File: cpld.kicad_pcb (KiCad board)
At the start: 2 copper layers, 30 parts, among them IC1 MCP1726-3302E_SN, IC2 EPM3064ATC44-7N, J1 USB_OTG, J2 INPUTS, J3 OUTPUTS, J4 Conn_ARM_JTAG_SWD_10, SW1 POWER_SW, SW2 SW_DIP_x01, SW3 SW_DIP_x01, SW4 SW_DIP_x01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

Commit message: Final PCB
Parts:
- removed SW4, SW5: SW_DIP_x01, Button_Switch_THT:SW_DIP_SPSTx01_Slide_9.78x4.72mm_W7.62mm_P2.54mm
- added C9: 0.1u, Capacitor_SMD:C_0603_1608Metric, F.Cu at (152.2, 93.3)
- added SW0: SW_DIP_x01, Button_Switch_THT:SW_DIP_SPSTx01_Slide_9.78x4.72mm_W7.62mm_P2.54mm, F.Cu at (180.3, 119.3)
- added SW_POW1: POWER_SW, Button_Switch_THT:SW_DIP_SPSTx01_Slide_9.78x4.72mm_W7.62mm_P2.54mm, F.Cu at (103.3, 107.7)
- C2: value 1000p -> 1u
- J2, J3: footprint Connector_PinSocket_2.54mm:PinSocket_2x16_P2.54mm_Vertical -> Connector_PinSocket_2.54mm:PinSocket_2x16_P2.54mm_Vertical_SMD; moved to B.Cu
- SW1: value POWER_SW -> SW_DIP_x01
- Y1: value ECS-2033-500-BN-TR3 -> ECS-TXO-3225-250-TR; footprint ECS2033:ECS2033500BNTR3 -> ECS_3225:OSC_ECS-TXO-3225-250-TR
- moved R6 61.1 mm to (123.3, 118.9), turned to -90 degrees
- moved SW1 55.1 mm to (170.3, 119.3), turned to 90 degrees
- moved J3 54.4 mm to (169.8, 68.0), turned to -90 degrees
- moved R7 50.9 mm to (170.3, 102.7), turned to -90 degrees
- moved SW2 49.0 mm to (160.3, 119.3), turned to 90 degrees
- moved D2 48.8 mm to (165.2, 101.8), turned to -90 degrees
- moved SW3 45.3 mm to (150.3, 119.3), turned to 90 degrees
- moved J1 44.5 mm to (91.0, 102.9), turned to -90 degrees
- moved R1 39.0 mm to (113.2, 102.4), turned to 90 degrees
- moved C2 27.0 mm to (129.2, 102.1), turned to 90 degrees
- moved R4 26.8 mm to (124.2, 87.0), turned to 90 degrees
- moved R3 25.8 mm to (121.2, 87.0), turned to -90 degrees
- moved R8 24.8 mm to (138.9, 98.0), turned to -90 degrees
- moved C4 23.8 mm to (138.9, 101.6), turned to -90 degrees
- moved C1 23.4 mm to (96.2, 100.8), turned to -90 degrees
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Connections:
- D1 pad 1: GND -> Net-(D1-Pad1)
- D1 pad 2: Net-(D1-Pad2) -> /POWER_LED
- D2 pad 1: GND -> Net-(D2-Pad1)
- D2 pad 2: Net-(D2-Pad2) -> /STATUS_LED
- IC2 pad 1: /TDI -> /DI0/TDI
- IC2 pad 10: /DI5 -> /DI7
- IC2 pad 12: /DI6 -> /DI8
- IC2 pad 13: /DI7 -> /DI9
- IC2 pad 14: /DI8 -> /DI10
- IC2 pad 15: /DI9 -> /DI11
- IC2 pad 18: /DO0 -> /DI12
- IC2 pad 19: /DO1 -> /DO0
- IC2 pad 2: /DI0 -> /DI1
- IC2 pad 20: /DO2 -> /DO1
- IC2 pad 21: /DO3 -> /DO2
- IC2 pad 22: /DO4 -> /DO3
- IC2 pad 23: /DO5 -> /DO4
- IC2 pad 25: /DO6 -> /DO5
- IC2 pad 26: /TCK -> /DO6/TCK
- IC2 pad 28: /DO8 -> /DO9
- IC2 pad 3: /DI1 -> /DI2
- IC2 pad 31: /DO9 -> /DO10
- IC2 pad 32: /TDO -> /DO11/TDO
- IC2 pad 33: unconnected-(IC2-Pad33) -> /DO12
- IC2 pad 34: /SW_B0 -> /STATUS_LED
- IC2 pad 35: /SW_B1 -> /SW_B0
- IC2 pad 42: /SW_B2 -> /SW_B1
- IC2 pad 43: /SW_B3 -> /SW_B2
- IC2 pad 44: unconnected-(IC2-Pad44) -> /SW_B3
- IC2 pad 5: /DI2 -> /DI3
- IC2 pad 6: /DI3 -> /DI4
- IC2 pad 7: /TMS -> /DI5/TMS
- IC2 pad 8: /DI4 -> /DI6
- J2 pad 1: /DI0 -> /DI0/TDI
- J2 pad 10: /DI9 -> GND
- J2 pad 11: unconnected-(J2-Pad11) -> /DI5/TMS
- J2 pad 12: unconnected-(J2-Pad12) -> GND
- J2 pad 13: unconnected-(J2-Pad13) -> /DI6
- J2 pad 14: unconnected-(J2-Pad14) -> GND
- J2 pad 15: unconnected-(J2-Pad15) -> /DI7
- J2 pad 16: unconnected-(J2-Pad16) -> GND
- J2 pad 17: GND -> /DI8
- J2 pad 19: GND -> /DI9
- J2 pad 2: /DI1 -> GND
- J2 pad 21: GND -> /DI10
- J2 pad 23: GND -> /DI11
- J2 pad 25: GND -> /DI12
- J2 pad 27: GND -> unconnected-(J2-Pad27)
- J2 pad 29: GND -> unconnected-(J2-Pad29)
- J2 pad 3: /DI2 -> /DI1
- J2 pad 31: GND -> unconnected-(J2-Pad31)
- J2 pad 4: /DI3 -> GND
- J2 pad 5: /DI4 -> /DI2
- J2 pad 6: /DI5 -> GND
- J2 pad 7: /DI6 -> /DI3
- J2 pad 8: /DI7 -> GND
- J2 pad 9: /DI8 -> /DI4
- J3 pad 10: /DO9 -> GND
- J3 pad 11: unconnected-(J3-Pad11) -> /DO5
- J3 pad 12: unconnected-(J3-Pad12) -> GND
- J3 pad 13: unconnected-(J3-Pad13) -> /DO6/TCK
- J3 pad 14: unconnected-(J3-Pad14) -> GND
- J3 pad 15: unconnected-(J3-Pad15) -> /DO7
- J3 pad 16: unconnected-(J3-Pad16) -> GND
- J3 pad 17: GND -> /DO8
- J3 pad 19: GND -> /DO9
- J3 pad 2: /DO1 -> GND
- J3 pad 21: GND -> /DO10
- J3 pad 23: GND -> /DO11/TDO
- J3 pad 25: GND -> /DO12
- J3 pad 27: GND -> unconnected-(J3-Pad27)
- J3 pad 29: GND -> unconnected-(J3-Pad29)
- J3 pad 3: /DO2 -> /DO1
- J3 pad 31: GND -> unconnected-(J3-Pad31)
- J3 pad 4: /DO3 -> GND
- J3 pad 5: /DO4 -> /DO2
- J3 pad 6: /DO5 -> GND
- J3 pad 7: /DO6 -> /DO3
- J3 pad 8: /DO7 -> GND
- J3 pad 9: /DO8 -> /DO4
- J4 pad 2: /TMS -> /DI5/TMS
- J4 pad 4: /TCK -> /DO6/TCK
- J4 pad 8: /TDI -> /DI0/TDI
- R2 pad 2: /TDO -> /DO11/TDO
- R3 pad 1: /TMS -> /DI5/TMS
- R4 pad 2: /TDO -> /DO11/TDO
- R5 pad 2: /TDI -> /DI0/TDI
- R6 pad 1: /POWER_LED -> Net-(D1-Pad1)
- R6 pad 2: Net-(D1-Pad2) -> GND
- R7 pad 1: /STATUS_LED -> Net-(D2-Pad1)
- R7 pad 2: Net-(D2-Pad2) -> GND
- R8 pad 1: /TCK -> /DO6/TCK
- SW1 pad 2: Net-(IC1-Pad3) -> /SW_B1
- SW2 pad 2: /SW_B0 -> /SW_B2
- SW3 pad 2: /SW_B1 -> /SW_B3
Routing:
- net +3.3V: track 0.00 -> 112.3 mm
- net /DI0/TDI: track 0.00 -> 108.6 mm, vias 0 -> 3
- net /DO11/TDO: track 0.00 -> 93.1 mm, vias 0 -> 5
- net /DO6/TCK: track 0.00 -> 90.2 mm, vias 0 -> 5
- net /DI5/TMS: track 0.00 -> 82.0 mm, vias 0 -> 3
- net GND: track 0.00 -> 72.2 mm, vias 0 -> 88
- net /DI1: track 0.00 -> 66.7 mm, vias 0 -> 1
- net /DI2: track 0.00 -> 64.2 mm, vias 0 -> 1
- net /DI3: track 0.00 -> 60.0 mm, vias 0 -> 1
- net /DO12: track 0.00 -> 57.8 mm, vias 0 -> 3
- net /DO5: track 0.00 -> 57.4 mm, vias 0 -> 3
- net /DO4: track 0.00 -> 57.0 mm, vias 0 -> 3
- net /DI4: track 0.00 -> 56.3 mm, vias 0 -> 1
- net /DO7: track 0.00 -> 55.9 mm, vias 0 -> 3
- net /DO10: track 0.00 -> 55.4 mm, vias 0 -> 3
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- added copper zone on B.Cu, net GND
- added copper zone on F.Cu, net GND
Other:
- board outline added: 105 x 72 mm

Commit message: Improved PCB layout
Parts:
- C9, IC2, Y1: moved to B.Cu
- J4: footprint Connector_PinSocket_2.54mm:PinSocket_2x05_P2.54mm_Vertical -> Connector_PinSocket_2.54mm:PinSocket_2x05_P2.54mm_Vertical_SMD
- moved SW0 48.7 mm to (183.8, 83.9), turned to -90 degrees
- moved R7 47.5 mm to (125.1, 87.9), turned to 0 degrees
- moved D2 46.6 mm to (120.8, 87.9), turned to 180 degrees
- moved SW3 44.2 mm to (153.8, 83.9), turned to -90 degrees
- moved SW1 37.9 mm to (173.8, 83.9), turned to -90 degrees
- moved R6 36.5 mm to (104.0, 87.9), turned to 180 degrees
- moved SW2 36.0 mm to (163.8, 83.9), turned to -90 degrees
- moved R4 32.0 mm to (147.3, 64.9), turned to -90 degrees
- moved R2 31.1 mm to (147.3, 68.3), turned to 90 degrees
- moved J4 30.3 mm to (141.1, 69.1), turned to 180 degrees
- moved D1 30.3 mm to (107.9, 87.9), turned to 0 degrees
- moved SW_POW1 25.5 mm to (99.4, 82.5)
- moved R1 23.6 mm to (110.7, 79.0)
- moved J1 23.4 mm to (91.2, 79.5)
- moved C1 23.4 mm to (96.0, 77.4)
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- renumbered SW3 to SW0, SW2 to SW1, SW1 to SW2, SW0 to SW3
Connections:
- D1 pad 2: /POWER_LED -> +5V
- IC1 pad 5: /POWER_LED -> /STATUS_LED
- IC2 pad 28: /DO9 -> /DO8
- IC2 pad 31: /DO10 -> /DO9
- IC2 pad 32: /DO11/TDO -> /DO10/TDO
- IC2 pad 33: /DO12 -> /DO11
- IC2 pad 34: /STATUS_LED -> /DO12
- IC2 pad 35: /SW_B0 -> /SW_B3
- IC2 pad 42: /SW_B1 -> /SW_B2
- IC2 pad 43: /SW_B2 -> /SW_B1
- IC2 pad 44: /SW_B3 -> /SW_B0
- J3 pad 21: /DO10 -> /DO10/TDO
- J3 pad 23: /DO11/TDO -> /DO11
- R2 pad 2: /DO11/TDO -> /DO10/TDO
- R4 pad 2: /DO11/TDO -> /DO10/TDO
- SW0 pad 2: /SW_B3 -> /SW_B0
- SW1 pad 2: /SW_B2 -> /SW_B1
- SW2 pad 2: /SW_B1 -> /SW_B2
- SW3 pad 2: /SW_B0 -> /SW_B3
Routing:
- net /DO11/TDO: track 93.1 -> 0.00 mm, vias 5 -> 0
- net /DO10/TDO: track 0.00 -> 75.9 mm, vias 0 -> 1
- net /DO10: track 55.4 -> 0.00 mm, vias 3 -> 0
- net /DO11: track 0.00 -> 46.1 mm
- net /SW_B3: track 53.3 -> 13.1 mm, vias 1 -> 0
- net /DO8: track 0.00 -> 35.9 mm
- net /DO4: track 57.0 -> 23.4 mm, vias 3 -> 0
- net /DO6/TCK: track 90.2 -> 57.7 mm, vias 5 -> 2
- net /DO5: track 57.4 -> 27.2 mm, vias 3 -> 0
- net /DO0: track 43.3 -> 14.0 mm, vias 3 -> 0
- net /DO1: track 42.6 -> 15.9 mm, vias 3 -> 0
- net /DO2: track 42.2 -> 17.8 mm, vias 3 -> 0
- net /DO7: track 55.9 -> 33.2 mm, vias 3 -> 0
- net /DO3: track 41.8 -> 19.7 mm, vias 3 -> 0
- net +3.3V: track 112.3 -> 91.2 mm, vias 0 -> 4
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- added copper zone on F.Cu, net +3.3V
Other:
- board size 105 x 72 mm -> 105 x 42.1 mm

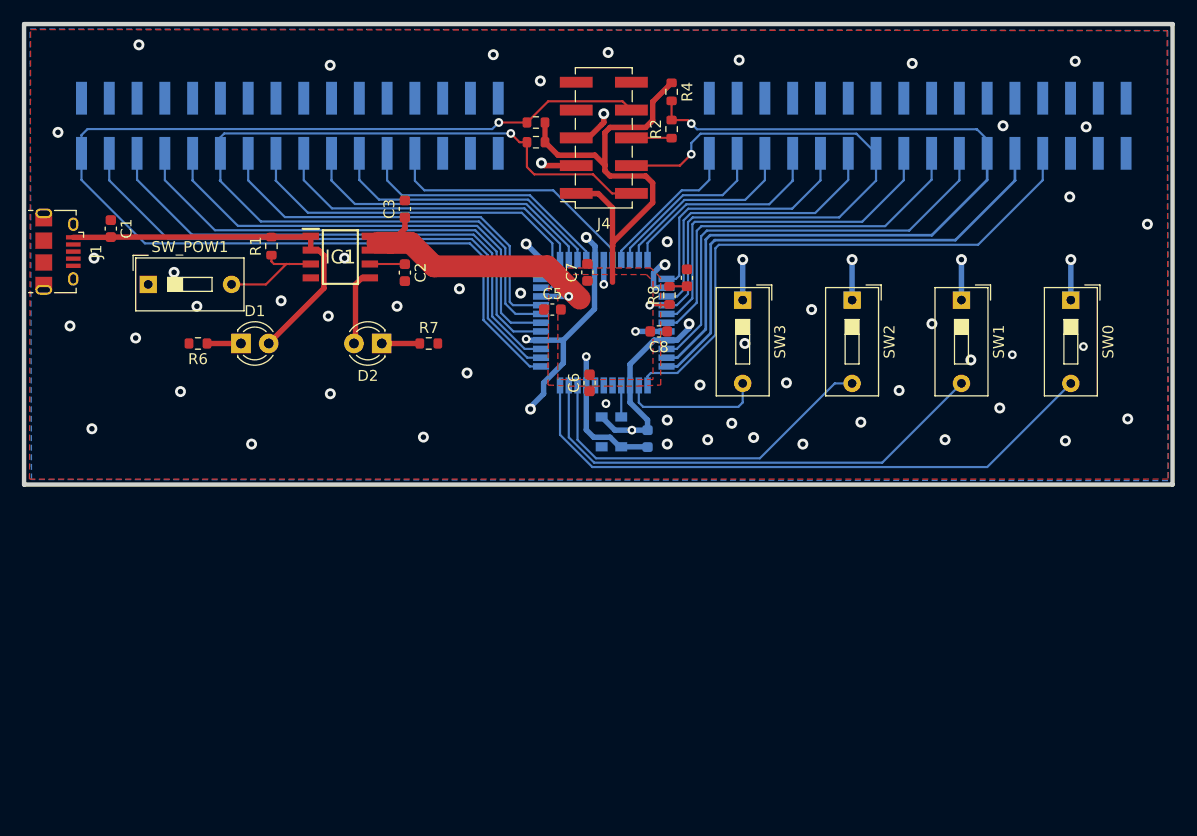
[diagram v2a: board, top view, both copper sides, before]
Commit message: Changed connectors and LDO
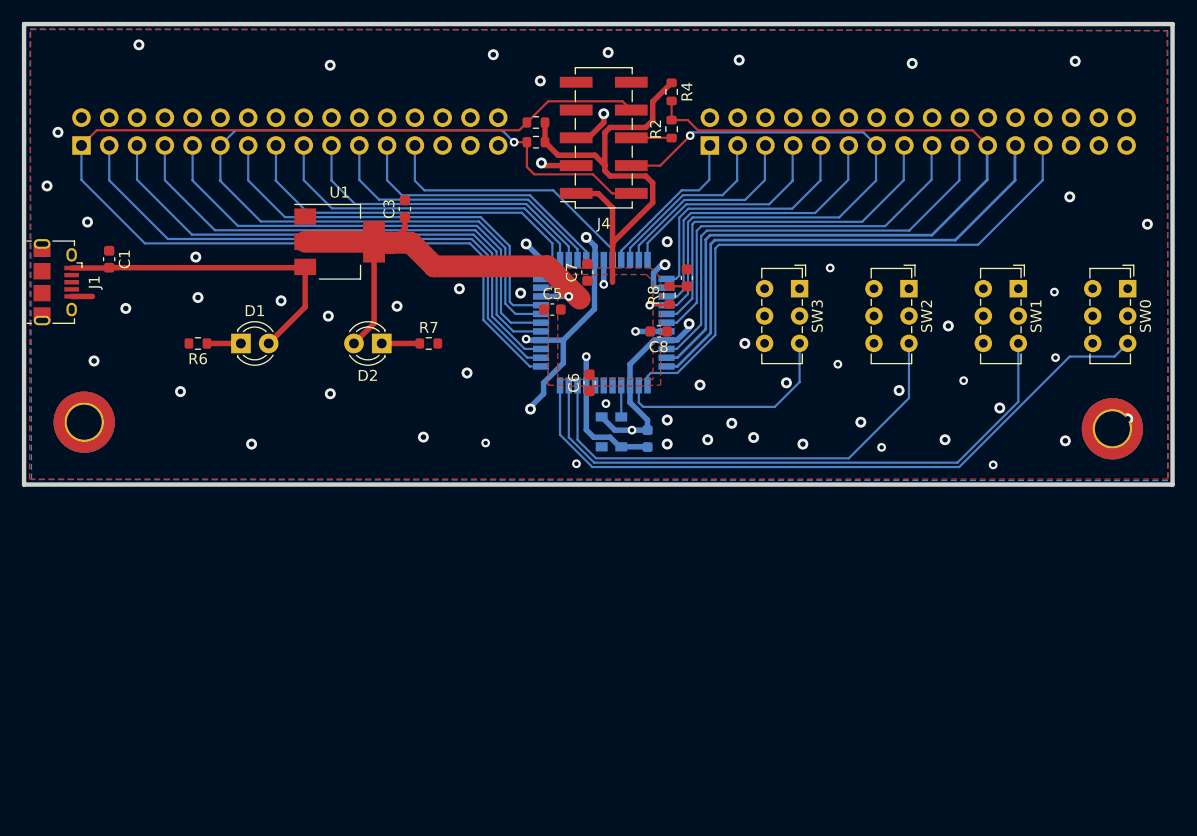
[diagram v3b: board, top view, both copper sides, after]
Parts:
- removed C2: 1u, Capacitor_SMD:C_0603_1608Metric
- removed IC1: MCP1726-3302E_SN, MCP1726:SOIC127P600X175-8N
- removed R1: 10k, Resistor_SMD:R_0603_1608Metric
- removed SW_POW1: POWER_SW, Button_Switch_THT:SW_DIP_SPSTx01_Slide_9.78x4.72mm_W7.62mm_P2.54mm
- added H2: MountingHole_Pad, MountingHole:MountingHole_3.2mm_M3_DIN965_Pad_TopBottom, F.Cu at (187.6, 95.7)
- added H4: MountingHole_Pad, MountingHole:MountingHole_3.2mm_M3_DIN965_Pad_TopBottom, F.Cu at (93.6, 95.1)
- added U1: AMS1117-3.3, Package_TO_SOT_SMD:SOT-223-3_TabPin2, F.Cu at (117.0, 78.6)
- C3: value 10u -> 22u
- J2, J3: footprint Connector_PinSocket_2.54mm:PinSocket_2x16_P2.54mm_Vertical_SMD -> Connector_PinSocket_2.54mm:PinSocket_2x16_P2.54mm_Vertical
- SW0, SW1, SW2, SW3: value SW_DIP_x01 -> SW_DPDT_x2; footprint Button_Switch_THT:SW_DIP_SPSTx01_Slide_9.78x4.72mm_W7.62mm_P2.54mm -> Button_Switch_THT:SW_E-Switch_EG1271_DPDT
- moved J2 19.1 mm to (93.3, 69.8)
- moved J3 19.1 mm to (150.8, 69.8)
- moved SW0 5.30 mm to (189.0, 82.9)
- moved SW1 5.30 mm to (179.0, 82.9)
- moved SW2 5.30 mm to (169.0, 82.9)
- moved SW3 5.30 mm to (159.0, 82.9)
- moved C1 2.80 mm to (95.9, 80.2)
- moved J1 2.80 mm to (91.0, 82.3)
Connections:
- D2 pad 2: /STATUS_LED -> +3.3V
- SW0 pad 1: GND -> unconnected-(SW0-Pad1)
- SW0 pad 2: /SW_B0 -> GND
- SW1 pad 1: GND -> unconnected-(SW1-Pad1)
- SW1 pad 2: /SW_B1 -> GND
- SW2 pad 1: GND -> unconnected-(SW2-Pad1)
- SW2 pad 2: /SW_B2 -> GND
- SW3 pad 1: GND -> unconnected-(SW3-Pad1)
- SW3 pad 2: /SW_B3 -> GND
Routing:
- net GND: track 69.8 -> 56.9 mm, vias 65 -> 63
- net +3.3V: track 91.2 -> 103.2 mm
- net Net-(IC1-Pad3): track 10.1 -> 0.00 mm
- net /SW_B1: track 44.6 -> 54.4 mm
- net /SW_B2: track 33.6 -> 43.3 mm
- net /SW_B3: track 13.1 -> 20.9 mm
- net /STATUS_LED: track 7.42 -> 0.00 mm
- net /SW_B0: track 55.6 -> 62.3 mm
- net +5V: track 34.6 -> 29.8 mm
- net Net-(C2-Pad1): track 3.21 -> 0.00 mm
- net /DI0/TDI: track 108.4 -> 107.2 mm, vias 1 -> 0
- net /DO6/TCK: track 57.7 -> 57.0 mm
- net /DI5/TMS: track 82.7 -> 83.2 mm
- net /DO10/TDO: track 75.9 -> 76.2 mm, vias 1 -> 0

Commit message: sent to the jlcpcb
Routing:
- net /DI5/TMS: track 83.2 -> 82.5 mm
- net /DO12: track 51.5 -> 52.2 mm
- net /DO4: track 23.4 -> 24.1 mm
- net /DO0: track 14.0 -> 14.7 mm
- net /DO8: track 35.9 -> 36.6 mm
- net /DO7: track 33.2 -> 33.9 mm
- net /DO5: track 27.2 -> 27.9 mm
- net /DO9: track 40.4 -> 41.1 mm
- net /DO2: track 17.8 -> 18.5 mm
- net /DO1: track 15.9 -> 16.7 mm
- net /DI9: track 27.9 -> 28.6 mm
- net /DI8: track 29.8 -> 30.5 mm
- net /DI7: track 35.2 -> 35.9 mm
- net /DI6: track 37.0 -> 37.7 mm
- net /DI3: track 45.9 -> 46.7 mm
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
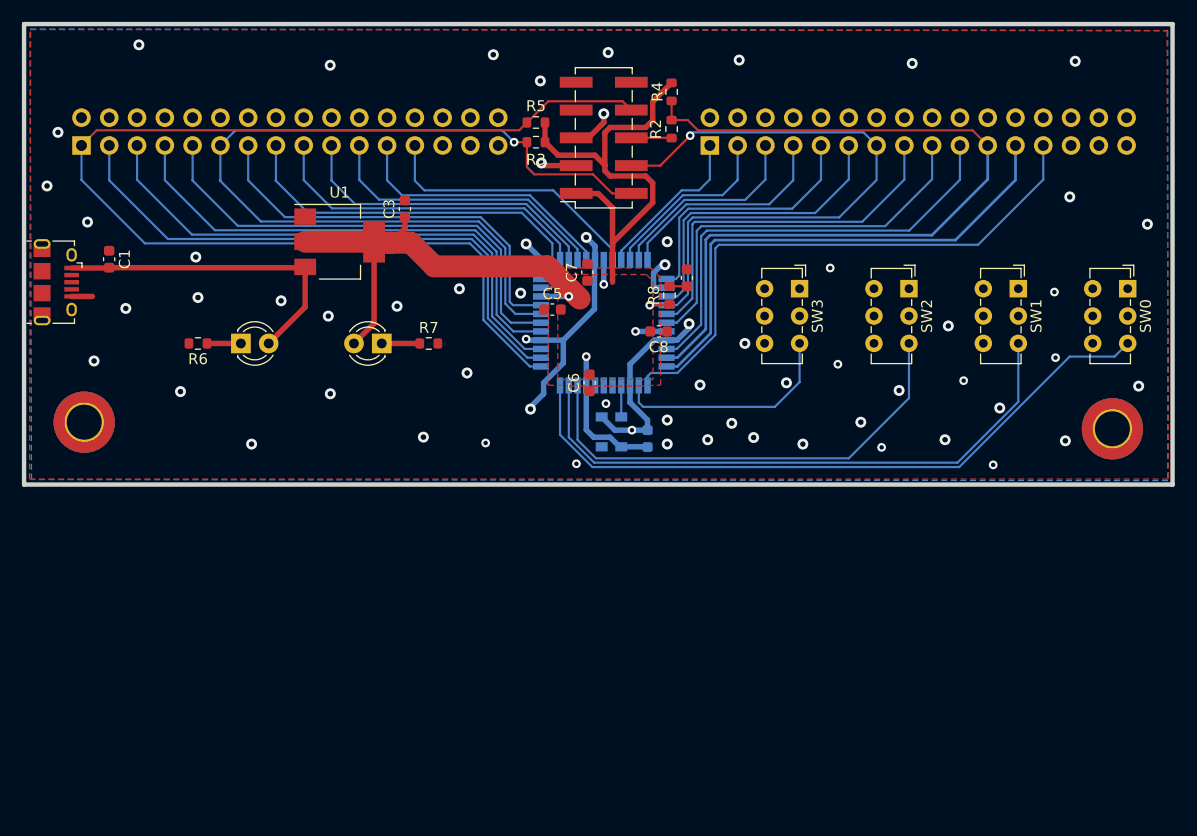
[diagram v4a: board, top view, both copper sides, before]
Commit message: added pullups for the switches
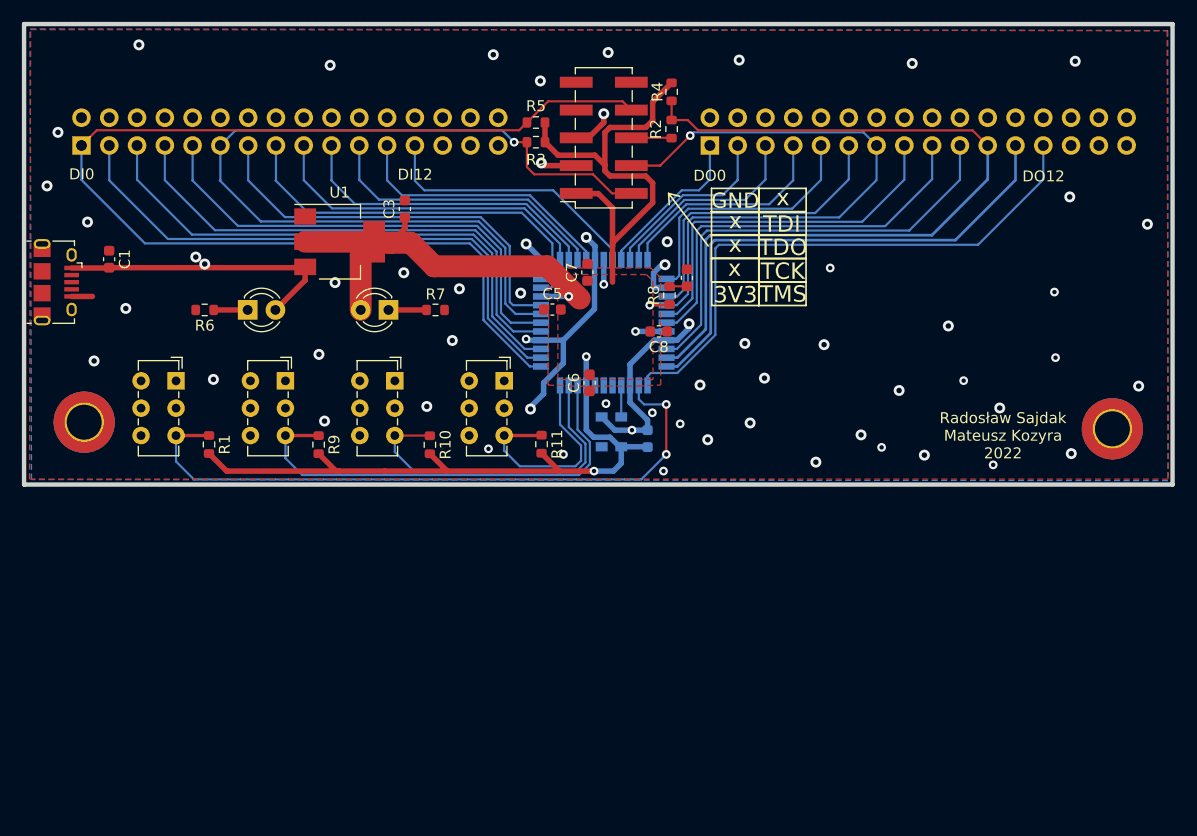
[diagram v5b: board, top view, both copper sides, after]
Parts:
- added R1: 10k, Resistor_SMD:R_0603_1608Metric, F.Cu at (105.0, 97.1)
- added R10: 10k, Resistor_SMD:R_0603_1608Metric, F.Cu at (125.2, 97.2)
- added R11: 10k, Resistor_SMD:R_0603_1608Metric, F.Cu at (135.4, 97.1)
- added R9: 10k, Resistor_SMD:R_0603_1608Metric, F.Cu at (115.0, 97.2)
- moved SW1 57.6 mm to (122.0, 91.3)
- moved SW2 57.6 mm to (112.0, 91.3)
- moved SW3 57.6 mm to (102.0, 91.3)
- moved SW0 57.6 mm to (132.0, 91.3)
- moved D1 3.13 mm to (108.5, 84.8)
- moved D2 3.13 mm to (121.4, 84.8)
- moved R6 3.13 mm to (104.6, 84.8)
- moved R7 3.13 mm to (125.7, 84.8)
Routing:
- net +3.3V: track 103.2 -> 147.1 mm, vias 4 -> 5
- net /SW_B0: track 62.3 -> 20.3 mm
- net /SW_B3: track 20.9 -> 60.4 mm, vias 0 -> 2
- net /SW_B1: track 54.4 -> 30.8 mm
- net +5V: track 29.8 -> 26.5 mm, vias 0 -> 1
- net /SW_B2: track 43.3 -> 41.6 mm
- net GND: vias 63 -> 61
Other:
- board text added: "3V3"
- board text added: "DI0"
- board text added: "DI12"
- board text added: "DO0"
- board text added: "DO12"
- board text added: "GND"
- board text added: "Radosław Sajdak Mateusz Kozyra 2022"
- board text added: "TCK"
- board text added: "TDI"
- board text added: "TDO"
- board text added: "TMS"
- board text added: "x"

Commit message: Studenty studentom
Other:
- board text added: "Radosław Sajdak Mateusz Kozyra 2022 ~ Studenty studentom ~"
- board text removed: "Radosław Sajdak Mateusz Kozyra 2022"
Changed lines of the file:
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@@
     (effects (font (size 1.4 1.4) (thickness 0.3)))
   )
-  (gr_text "Radosław Sajdak\nMateusz Kozyra\n2022" (at 177.6 96.33) (layer "F.SilkS")
+  (gr_text "Radosław Sajdak\nMateusz Kozyra\n2022\n~ Studenty studentom ~" (at 174.62 94.49) (layer "F.SilkS")
     (effects (font (size 1 1) (thickness 0.15)))
   )
@@
   (via (at 164.62 96.26) (size 1) (drill 0.5) (layers "F.Cu" "B.Cu") (free) (net 1))
   (via (at 134.4 93.9) (size 1) (drill 0.5) (layers "F.Cu" "B.Cu") (free) (net 1))
-  (via (at 166.5 97.4) (size 0.8) (drill 0.4) (layers "F.Cu" "B.Cu") (free) (net 1))
+  (via (at 166.01 98.65) (size 0.8) (drill 0.4) (layers "F.Cu" "B.Cu") (free) (net 1))
   (via (at 135.4 71.4) (size 1) (drill 0.5) (layers "F.Cu" "B.Cu") (net 1))
   (via (at 190.8 77) (size 1) (drill 0.5) (layers "F.Cu" "B.Cu") (net 1))
@@
   (via (at 98.6 60.6) (size 1) (drill 0.5) (layers "F.Cu" "B.Cu") (net 1))
   (via (at 116.085511 62.46728) (size 1) (drill 0.5) (layers "F.Cu" "B.Cu") (net 1))
-  (via (at 174 91.3) (size 0.8) (drill 0.4) (layers "F.Cu" "B.Cu") (free) (net 1))
+  (via (at 174.51 90.81) (size 0.8) (drill 0.4) (layers "F.Cu" "B.Cu") (free) (net 1))
   (via (at 143.675 95.825) (size 0.8) (drill 0.4) (layers "F.Cu" "B.Cu") (net 1))
   (via (at 183.7 74.5) (size 1) (drill 0.5) (layers "F.Cu" "B.Cu") (free) (net 1))
@@
   (via (at 146.7 80.7) (size 1) (drill 0.5) (layers "F.Cu" "B.Cu") (net 1))
   (via (at 170.41 98.11) (size 1) (drill 0.5) (layers "F.Cu" "B.Cu") (net 1))
-  (via (at 177.3 93.8) (size 1) (drill 0.5) (layers "F.Cu" "B.Cu") (free) (net 1))
+  (via (at 178.67 95.3) (size 1) (drill 0.5) (layers "F.Cu" "B.Cu") (free) (net 1))
   (via (at 115.57 94.996) (size 1) (drill 0.5) (layers "F.Cu" "B.Cu") (free) (net 1))
   (via (at 141.1 66.9) (size 1) (drill 0.5) (layers "F.Cu" "B.Cu") (net 1))
@@
   (via (at 148.9 86.1) (size 1) (drill 0.5) (layers "F.Cu" "B.Cu") (net 1))
   (via (at 153.477728 61.991895) (size 1) (drill 0.5) (layers "F.Cu" "B.Cu") (net 1))
-  (via (at 168.1 92.2) (size 1) (drill 0.5) (layers "F.Cu" "B.Cu") (free) (net 1))
+  (via (at 167.01 94.13) (size 1) (drill 0.5) (layers "F.Cu" "B.Cu") (free) (net 1))
   (via (at 184.2 62.1) (size 1) (drill 0.5) (layers "F.Cu" "B.Cu") (net 1))
   (segment (start 135.6 91.5) (end 135.6 92.5) (width 0.5) (layer "B.Cu") (net 1))
